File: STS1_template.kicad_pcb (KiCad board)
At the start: 4 copper layers, 85 x 85 mm, 68 parts, among them CON1 DISCO-CON1, CON11 DISCO-CON1, CON2 DISCO-CON2, CON21 DISCO-CON2, IC1 STM32F411RET6TR, IC2 STWD100PYW83F, J1 Conn_01x02_Female, J10 Conn_01x01_Male, J11 Conn_01x01_Male, J12 Conn_01x01_Male, J13 Conn_01x01_Male, J14 Conn_01x01_Male, J15 Conn_01x01_Male, J16 Conn_01x01_Male, J17 Conn_01x01_Male, J18 Conn_01x01_Male, J19 Conn_01x01_Male, J2 Conn_01x05_Female, J20 Conn_01x01_Male, J21 Conn_01x01_Male, J22 Conn_01x01_Male, J23 Conn_01x01_Male, J24 Conn_01x01_Male, J25 Conn_01x01_Male, J3 Conn_01x01_Male, J4 Conn_01x01_Male, J5 Conn_01x01_Male, J6 Conn_01x01_Male, J7 Conn_01x01_Male, J8 Conn_01x01_Male, J9 Conn_01x01_Male, U1 coordinate_system

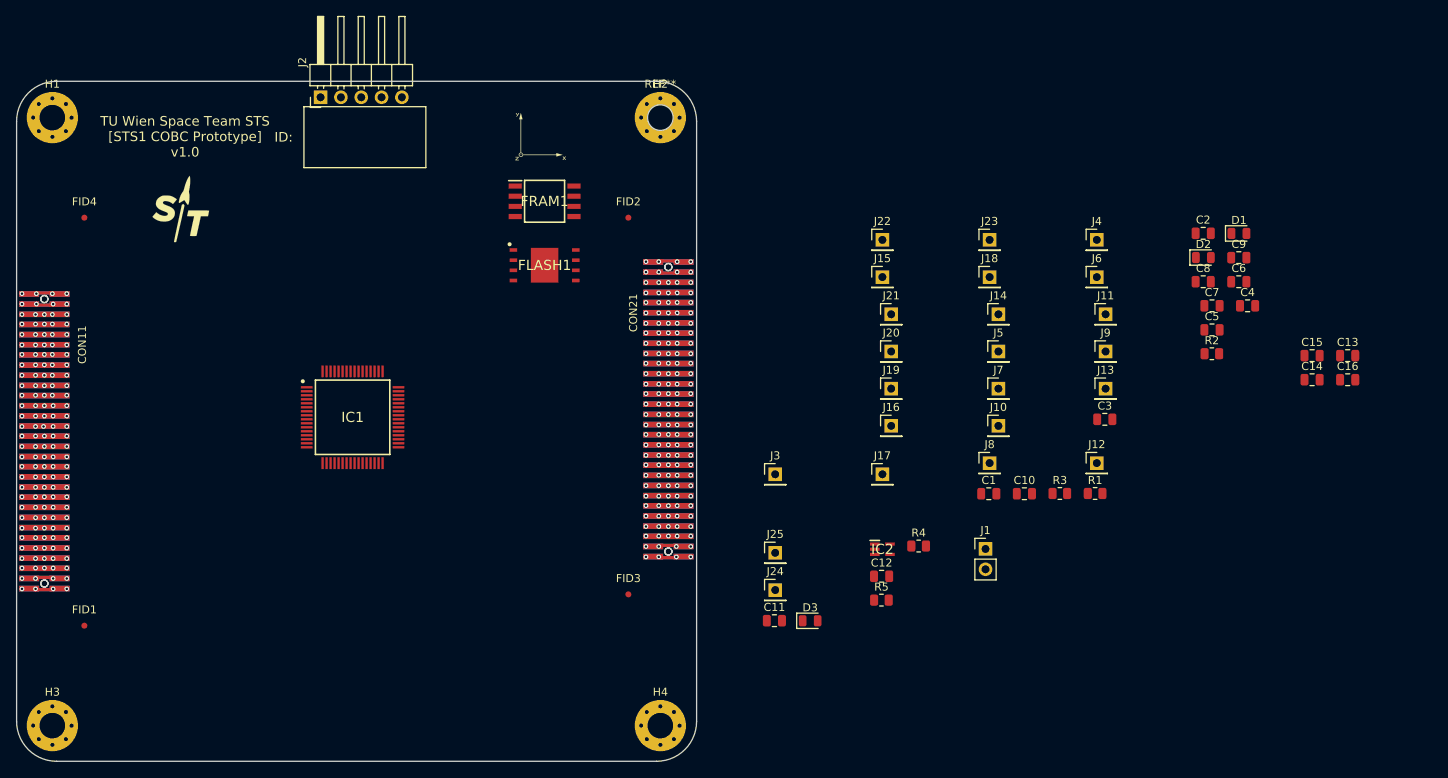
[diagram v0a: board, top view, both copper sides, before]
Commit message: Add reference layout for dcdc
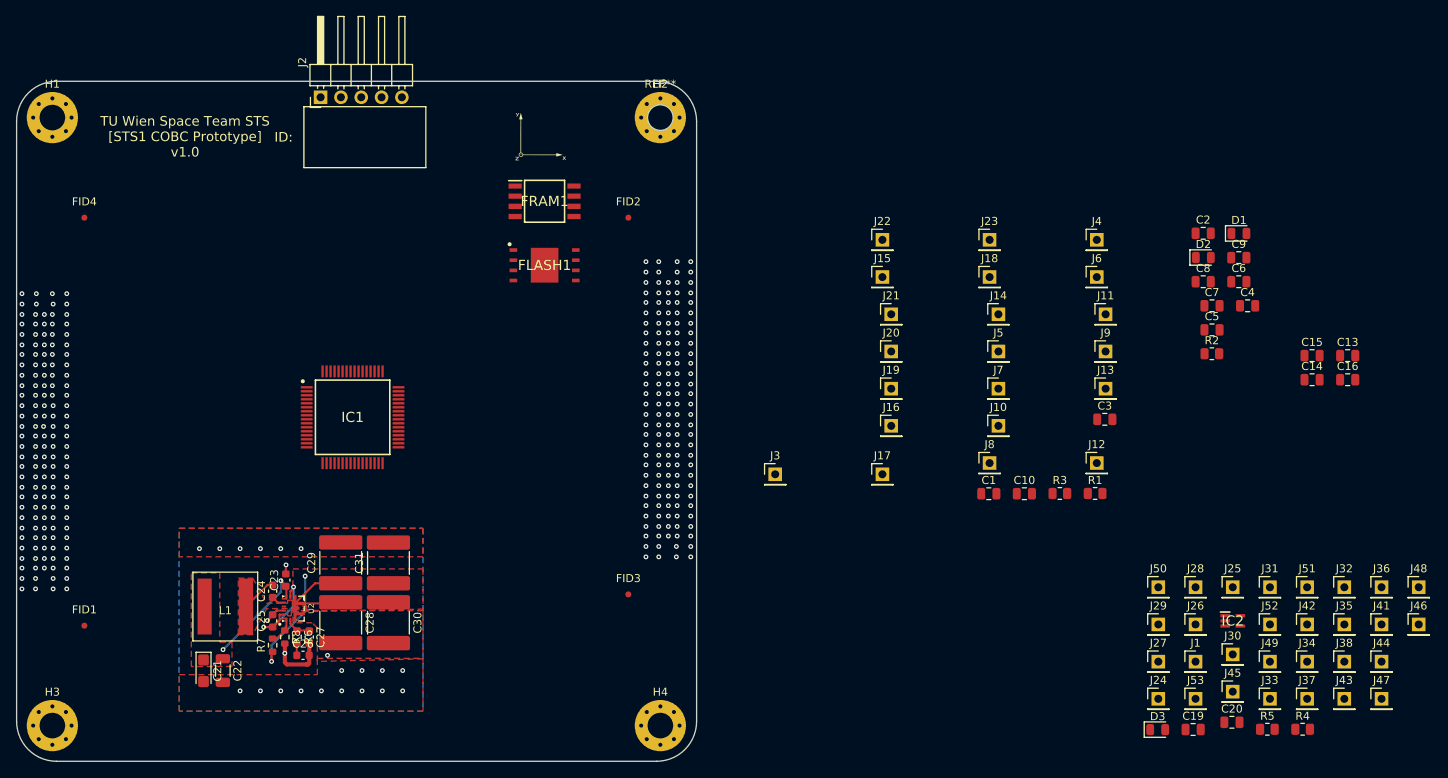
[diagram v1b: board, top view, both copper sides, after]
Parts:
- removed C11: 100n, Capacitor_SMD:C_0805_2012Metric
- removed C12: 47u, Capacitor_SMD:C_0805_2012Metric
- removed CON1, CON11: DISCO-CON1, cubesatFunkmodul:Cubesatconnector
- removed CON2, CON21: DISCO-CON2, cubesatFunkmodul:Cubesatconnector
- removed G***: LOGO, spaceteam:STLogo
- added C19: 100n, Capacitor_SMD:C_0805_2012Metric, F.Cu at (262.0, 122.8)
- added C20: 47u, Capacitor_SMD:C_0805_2012Metric, F.Cu at (266.8, 121.9)
- added C21: 47uF, Capacitor_Tantalum_SMD:CP_EIA-3216-18_Kemet-A, F.Cu at (138.3, 115.5)
- added C22: 10uF, Capacitor_SMD:C_1206_3216Metric, F.Cu at (140.7, 115.5)
- added C23: 100nF, Capacitor_SMD:C_0603_1608Metric, F.Cu at (148.6, 104.2)
- added C24: 150nF, Capacitor_SMD:C_0603_1608Metric, F.Cu at (146.9, 105.5)
- added C25: 2.2uF, Capacitor_SMD:C_0603_1608Metric, F.Cu at (146.9, 109.2)
- added C26: 39nF, Capacitor_SMD:C_0603_1608Metric, F.Cu at (150.7, 113.6)
- added C27: 82pF, Capacitor_SMD:C_0603_1608Metric, F.Cu at (151.5, 111.3)
- added C28: 68uF, Capacitor_SMD:C_2220_5650Metric, F.Cu at (155.4, 109.5)
- added C29: 68uF, Capacitor_SMD:C_2220_5650Metric, F.Cu at (155.4, 102.0)
- added C30: 68uF, Capacitor_SMD:C_2220_5650Metric, F.Cu at (161.4, 109.5)
- added C31: 68uF, Capacitor_SMD:C_2220_5650Metric, F.Cu at (161.4, 102.0)
- added J26: Conn_01x01_Male, Connector_PinHeader_2.54mm:PinHeader_1x01_P2.54mm_Vertical, F.Cu at (262.3, 109.7)
- added J27: Conn_01x01_Male, Connector_PinHeader_2.54mm:PinHeader_1x01_P2.54mm_Vertical, F.Cu at (257.6, 114.3)
- added J28: Conn_01x01_Male, Connector_PinHeader_2.54mm:PinHeader_1x01_P2.54mm_Vertical, F.Cu at (262.3, 105.0)
- added J29: Conn_01x01_Male, Connector_PinHeader_2.54mm:PinHeader_1x01_P2.54mm_Vertical, F.Cu at (257.6, 109.7)
- added J30: Conn_01x01_Male, Connector_PinHeader_2.54mm:PinHeader_1x01_P2.54mm_Vertical, F.Cu at (266.9, 113.4)
- added J31: Conn_01x01_Male, Connector_PinHeader_2.54mm:PinHeader_1x01_P2.54mm_Vertical, F.Cu at (271.6, 105.0)
- added J32: Conn_01x01_Male, Connector_PinHeader_2.54mm:PinHeader_1x01_P2.54mm_Vertical, F.Cu at (280.9, 105.0)
- added J33: Conn_01x01_Male, Connector_PinHeader_2.54mm:PinHeader_1x01_P2.54mm_Vertical, F.Cu at (271.6, 119.0)
- added J34: Conn_01x01_Male, Connector_PinHeader_2.54mm:PinHeader_1x01_P2.54mm_Vertical, F.Cu at (276.2, 114.3)
- added J35: Conn_01x01_Male, Connector_PinHeader_2.54mm:PinHeader_1x01_P2.54mm_Vertical, F.Cu at (280.9, 109.7)
- added J36: Conn_01x01_Male, Connector_PinHeader_2.54mm:PinHeader_1x01_P2.54mm_Vertical, F.Cu at (285.5, 105.0)
- added J37: Conn_01x01_Male, Connector_PinHeader_2.54mm:PinHeader_1x01_P2.54mm_Vertical, F.Cu at (276.2, 119.0)
- added J38: Conn_01x01_Male, Connector_PinHeader_2.54mm:PinHeader_1x01_P2.54mm_Vertical, F.Cu at (280.9, 114.3)
- added J41: Conn_01x01_Male, Connector_PinHeader_2.54mm:PinHeader_1x01_P2.54mm_Vertical, F.Cu at (285.5, 109.7)
- added J42: Conn_01x01_Male, Connector_PinHeader_2.54mm:PinHeader_1x01_P2.54mm_Vertical, F.Cu at (276.2, 109.7)
- added J43: Conn_01x01_Male, Connector_PinHeader_2.54mm:PinHeader_1x01_P2.54mm_Vertical, F.Cu at (280.9, 119.0)
- added J44: Conn_01x01_Male, Connector_PinHeader_2.54mm:PinHeader_1x01_P2.54mm_Vertical, F.Cu at (285.5, 114.3)
- added J45: Conn_01x01_Male, Connector_PinHeader_2.54mm:PinHeader_1x01_P2.54mm_Vertical, F.Cu at (266.9, 118.1)
- added J46: Conn_01x01_Male, Connector_PinHeader_2.54mm:PinHeader_1x01_P2.54mm_Vertical, F.Cu at (290.2, 109.7)
- added J47: Conn_01x01_Male, Connector_PinHeader_2.54mm:PinHeader_1x01_P2.54mm_Vertical, F.Cu at (285.5, 119.0)
- added J48: Conn_01x01_Male, Connector_PinHeader_2.54mm:PinHeader_1x01_P2.54mm_Vertical, F.Cu at (290.2, 105.0)
- added J49: Conn_01x01_Male, Connector_PinHeader_2.54mm:PinHeader_1x01_P2.54mm_Vertical, F.Cu at (271.6, 114.3)
- added J50: Conn_01x01_Male, Connector_PinHeader_2.54mm:PinHeader_1x01_P2.54mm_Vertical, F.Cu at (257.6, 105.0)
- added J51: Conn_01x01_Male, Connector_PinHeader_2.54mm:PinHeader_1x01_P2.54mm_Vertical, F.Cu at (276.2, 105.0)
- added J52: Conn_01x01_Male, Connector_PinHeader_2.54mm:PinHeader_1x01_P2.54mm_Vertical, F.Cu at (271.6, 109.7)
- added J53: Conn_01x01_Male, Connector_PinHeader_2.54mm:PinHeader_1x01_P2.54mm_Vertical, F.Cu at (262.3, 119.0)
- added L1: 1uH, STS1_DCDC:XAL8080, F.Cu at (141.0, 107.5)
- added R6: 48k7, Resistor_SMD:R_0603_1608Metric, F.Cu at (150.0, 111.3)
- added R7: 357k, Resistor_SMD:R_0603_1608Metric, F.Cu at (146.9, 112.3)
- added R8: 48k7, Resistor_SMD:R_0603_1608Metric, F.Cu at (148.4, 111.3)
- added U2: TPS61288, STS1_DCDC:VQFN-HR, F.Cu at (149.5, 107.7)
- J1: value Conn_01x02_Female -> Conn_01x01_Male; footprint Connector_PinHeader_2.54mm:PinHeader_1x02_P2.54mm_Vertical -> Connector_PinHeader_2.54mm:PinHeader_1x01_P2.54mm_Vertical
- moved J25 57.4 mm to (266.9, 105.0)
- moved R4 53.2 mm to (275.7, 122.8)
- moved R5 50.9 mm to (271.2, 122.8)
- moved J24 49.8 mm to (257.6, 119.0)
- moved D3 45.5 mm to (257.5, 122.8)
- moved IC2 44.7 mm to (266.9, 109.2)
- moved J1 29.8 mm to (262.3, 114.3)
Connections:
- C10 pad 1: /STS1_RF/LoRa_VCC -> /STS1_COBC_Memories/FRAM_PowerSupply
- C13 pad 1: /STS1_RF/LoRa_VCC -> /STS1_COBC_Memories/FRAM_PowerSupply
- C14 pad 1: /STS1_RF/LoRa_VCC -> /STS1_COBC_Memories/FRAM_PowerSupply
- C15 pad 1: /STS1_RF/LoRa_VCC -> /STS1_COBC_Memories/FRAM_PowerSupply
- C16 pad 1: /STS1_RF/LoRa_VCC -> /STS1_COBC_Memories/FRAM_PowerSupply
- C5 pad 2: /STS1_RF/LoRa_VCC -> /STS1_COBC_Memories/FRAM_PowerSupply
- C6 pad 2: /STS1_RF/LoRa_VCC -> /STS1_COBC_Memories/FRAM_PowerSupply
- C7 pad 2: /STS1_RF/LoRa_VCC -> /STS1_COBC_Memories/FRAM_PowerSupply
- C9 pad 1: /STS1_RF/LoRa_VCC -> /STS1_COBC_Memories/FRAM_PowerSupply
- FLASH1 pad 3: Net-(FLASH1-Pad3) -> /STS1_COBC_Memories/Flash_WP
- FLASH1 pad 7: /STS1_COBC_Memories/Flash_PowerSupply -> Net-(FLASH1-Pad7)
- FLASH1 pad 8: /STS1_COBC_Memories/Flash_PowerSupply -> /STS1_COBC_Memories/FRAM_PowerSupply
- FRAM1 pad 1: GND -> /STS1_COBC_Memories/FRAM_CS
- FRAM1 pad 3: GND -> /STS1_COBC_Memories/FRAM_WP
- FRAM1 pad 4: /STS1_COBC_Memories/FRAM_PowerSupply -> GND
- FRAM1 pad 8: GND -> /STS1_COBC_Memories/FRAM_PowerSupply
- IC1 pad 1: /STS1_RF/LoRa_VCC -> /STS1_COBC_Memories/FRAM_PowerSupply
- IC1 pad 19: /STS1_RF/LoRa_VCC -> /STS1_COBC_Memories/FRAM_PowerSupply
- IC1 pad 2: Net-(IC1-Pad2) -> /STS1_COBC_uC/PC13
- IC1 pad 24: Net-(IC1-Pad24) -> /STS1_COBC_Memories/Flash_WP
- IC1 pad 3: Net-(IC1-Pad3) -> /STS1_COBC_uC/PC14
- IC1 pad 32: /STS1_RF/LoRa_VCC -> /STS1_COBC_Memories/FRAM_PowerSupply
- IC1 pad 4: Net-(IC1-Pad4) -> /STS1_COBC_uC/PC15
- IC1 pad 48: /STS1_RF/LoRa_VCC -> /STS1_COBC_Memories/FRAM_PowerSupply
- IC1 pad 50: Net-(IC1-Pad50) -> /STS1_COBC_uC/PA15
- IC1 pad 54: Net-(IC1-Pad54) -> /STS1_COBC_uC/PD2
- IC1 pad 55: Net-(IC1-Pad55) -> /STS1_COBC_uC/PB3
- IC1 pad 56: Net-(IC1-Pad56) -> /STS1_COBC_uC/PB4
- IC1 pad 57: Net-(IC1-Pad57) -> /STS1_COBC_uC/PB5
- IC1 pad 58: Net-(IC1-Pad58) -> /STS1_COBC_uC/PB6
- IC1 pad 59: Net-(IC1-Pad59) -> /STS1_COBC_uC/PB7
- IC1 pad 61: Net-(IC1-Pad61) -> /STS1_COBC_uC/PB9
- IC1 pad 62: /STS1_COBC_uC/SPI2_NSS -> /STS1_COBC_Memories/FRAM_CS
- IC1 pad 64: /STS1_RF/LoRa_VCC -> /STS1_COBC_Memories/FRAM_PowerSupply
- IC1 pad 8: Net-(IC1-Pad8) -> /STS1_COBC_uC/PC0
- IC1 pad 9: Net-(IC1-Pad9) -> /STS1_COBC_uC/PC1
- IC2 pad 5: /STS1_RF/LoRa_VCC -> /STS1_COBC_Memories/FRAM_PowerSupply
- J1 pad 1: GND -> Net-(IC1-Pad16)
- J11 pad 1: /STS1_COBC_uC/SPI2_NSS -> /STS1_COBC_Memories/FRAM_CS
- J16 pad 1: /STS1_RF/LoRa_VCC -> /STS1_COBC_Memories/FRAM_PowerSupply
- J18 pad 1: /STS1_RF/LoRa_VCC -> /STS1_COBC_Memories/FRAM_PowerSupply
- J2 pad 1: /STS1_RF/LoRa_VCC -> /STS1_COBC_Memories/FRAM_PowerSupply
- J24 pad 1: /STS1_COBC_uC/STM32_PA9(Watchdog_toggle) -> /STS1_COBC_uC/PA15
- J25 pad 1: /STS1_RF/LoRa_VCC -> /STS1_COBC_uC/PD2
- J7 pad 1: /STS1_RF/LoRa_VCC -> /STS1_COBC_Memories/FRAM_PowerSupply
- J8 pad 1: /STS1_RF/LoRa_VCC -> /STS1_COBC_Memories/FRAM_PowerSupply
- R5 pad 2: /STS1_RF/LoRa_VCC -> /STS1_COBC_Memories/FRAM_PowerSupply
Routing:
- net +5V: track 0.00 -> 26.2 mm, vias 0 -> 2
- net /STS1_PowerRegulation/VIN: track 0.00 -> 14.1 mm, vias 0 -> 2
- net Net-(C25-Pad1): track 0.00 -> 12.2 mm, vias 0 -> 2
- net GND: track 0.00 -> 11.9 mm, vias 35 -> 58
- net Net-(C24-Pad2): track 0.00 -> 4.45 mm
- net Net-(R7-Pad2): track 0.00 -> 3.52 mm
- net Net-(C27-Pad1): track 0.00 -> 3.19 mm
- net Net-(C24-Pad1): track 0.00 -> 1.69 mm
- net Net-(C26-Pad1): track 0.00 -> 1.47 mm
- added copper zone on F.Cu, net +5V
- added copper zone on F.Cu, net /STS1_PowerRegulation/VIN
- added copper zone on B.Cu, net GND
- added copper zone on F.Cu, net GND
- added copper zone on F.Cu, net Net-(C24-Pad2)
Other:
- rule pad_to_mask_clearance: 0.19 -> 0
